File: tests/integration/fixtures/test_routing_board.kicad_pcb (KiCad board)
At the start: 2 copper layers, 3 parts, among them U1 IC1

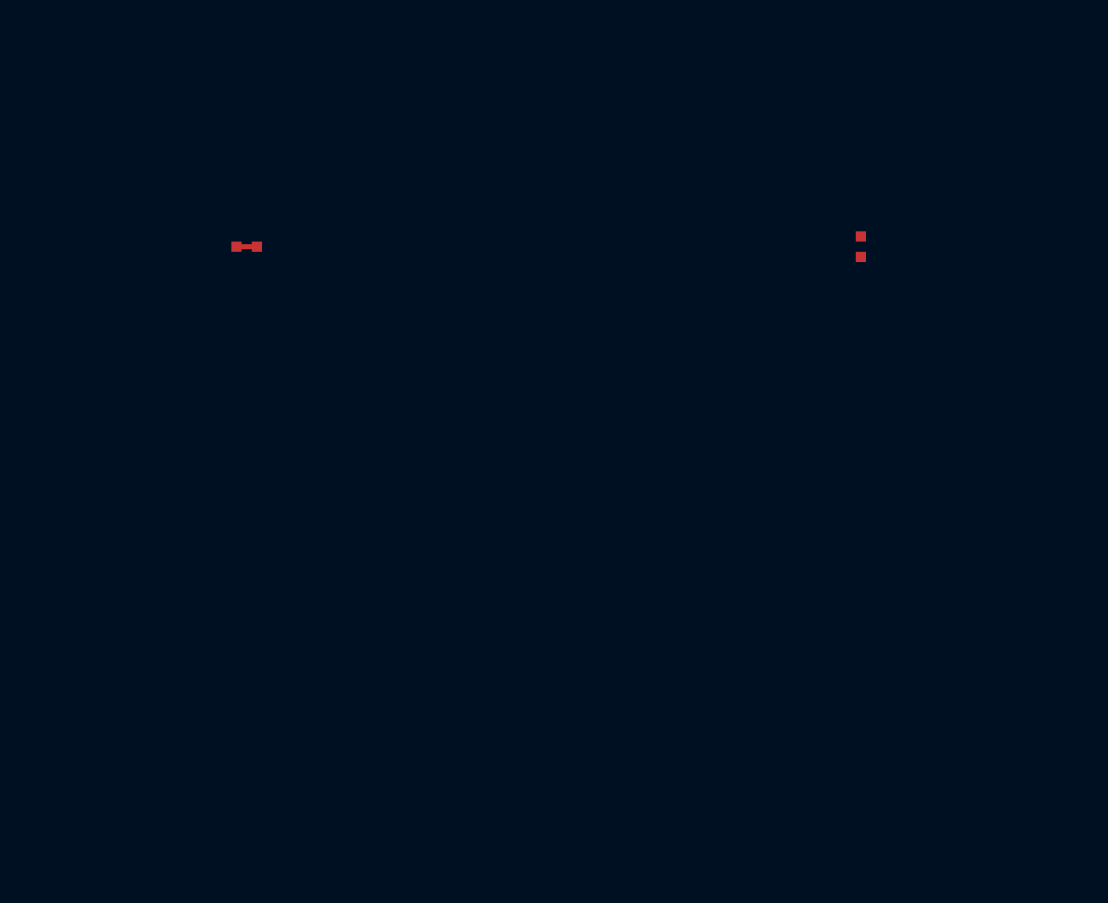
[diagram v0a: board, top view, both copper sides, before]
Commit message: Tighten PNS router error reporting and bounds checking
Replace silent DRC fallbacks with explicit exceptions: the previous
behaviour of _default_track_width and _default_clearance was to swallow
missing or malformed .kicad_pro data and return 0.25 mm / 0.2 mm. That
hides file corruption and makes the AI produce tracks at the wrong
width. Introduce four named exception classes (ProFileMissing,
ProFileMalformed, NetClassUnresolved, DesignRulesUnavailable) and
translate them into RouteFailure with a fix-it hint at the
auto_route_pair boundary. The user can still opt out by passing width=
and clearance= explicitly.

Add _check_segments_in_board and call it after postprocess. When the PCB
has Edge.Cuts, segments whose centerline + width/2 crosses the board
boundary raise RouteFailure (this is a router bug, never papered over).
When Edge.Cuts is absent, log a warning and proceed: the board outline
is a workflow artifact and may legitimately be missing mid-iteration;
KiCad's DRC owns the final validation.

Fixture: add a 50x40 mm gr_rect on Edge.Cuts so the new check is
exercised by the existing integration tests.

Tests: 21 new unit tests in tests/unit/router/test_router.py covering
every DRC exception path, the explicit-override escape hatch, and
boundary / non-boundary / degenerate / too-wide cases for
_check_segments_in_board.

Co-authored-by: Copilot <223556219+Copilot@users.noreply.github.com>

Signed-off-by: paul356 <panhao356@gmail.com>
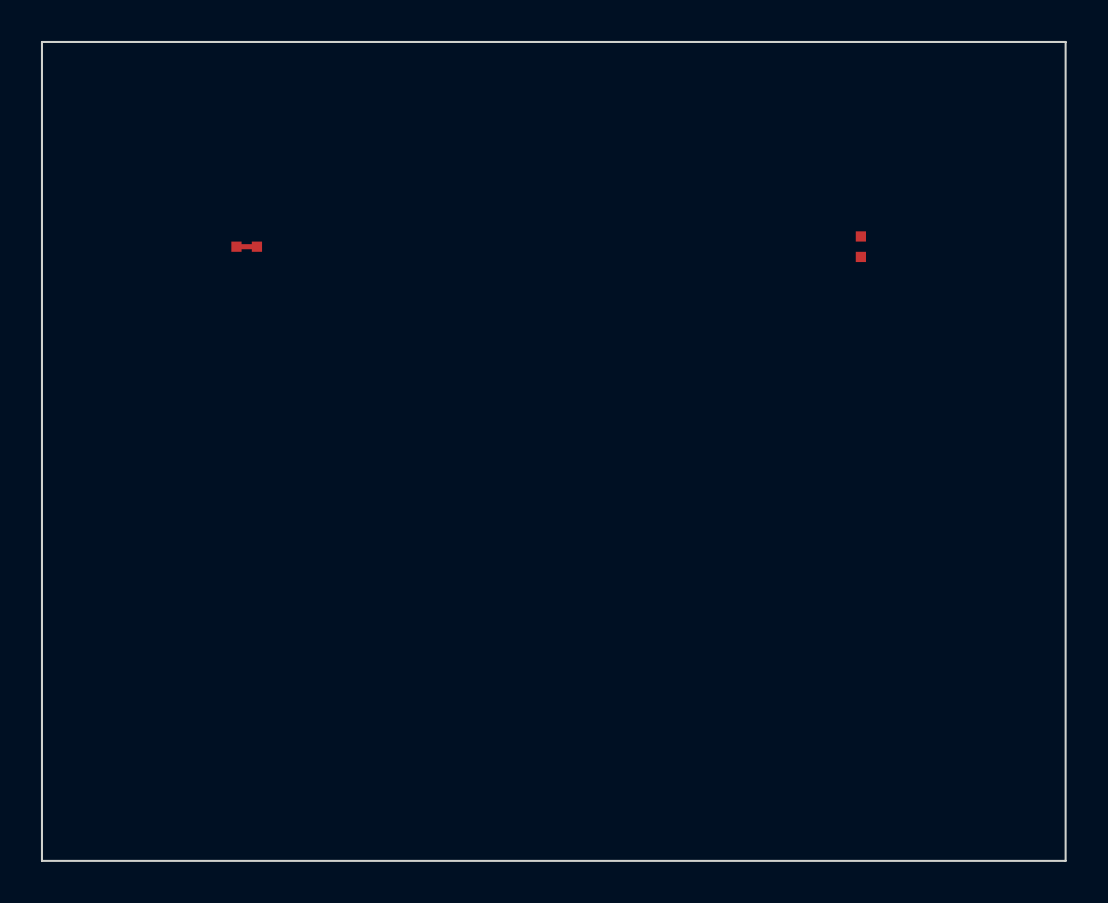
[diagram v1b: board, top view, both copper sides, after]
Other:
- board outline added: 50 x 40 mm
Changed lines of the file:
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@@
 		)
 	)
+	(gr_rect
+		(start 20.0 20.0)
+		(end 70.0 60.0)
+		(stroke
+			(width 0.1)
+			(type solid)
+		)
+		(fill none)
+		(layer "Edge.Cuts")
+		(uuid "edge-cuts-rect-0000")
+	)
 )

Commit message: feat(router): multi-layer MCP tool args + In1.Cu fixture footprint
- pcb_route_pad_to_pad: accept target_layer and via_pairs; emits
  vias in addition to segments; reports layers_used
- fixture: add In1.Cu copper layer and D1 footprint with pad 1 on
  In1.Cu (GND) for cross-layer routing tests

Co-authored-by: Copilot <223556219+Copilot@users.noreply.github.com>

Signed-off-by: paul356 <panhao356@gmail.com>
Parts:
- added D1: D1, Resistor_SMD:R_0402_1005Metric, In1.Cu at (60.0, 50.0)
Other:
- copper layers 2 -> 3
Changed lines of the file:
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@@
 		(0 "F.Cu" signal)
 		(31 "B.Cu" signal)
+		(33 "In1.Cu" signal)
 		(36 "B.Courtyard" user)
 		(37 "F.Courtyard" user)
@@
 		(uuid "edge-cuts-rect-0000")
 	)
+	# ---- D1: SMD pad on In1.Cu (GND) for cross-layer routing tests ----
+	(footprint "Resistor_SMD:R_0402_1005Metric"
+		(layer "In1.Cu")
+		(at 60.0 50.0 0.0)
+		(property "Reference" "D1")
+		(property "Value" "D1")
+		(fp_line
+			(start -1.05 -0.6)
+			(end 1.05 -0.6)
+			(layer "F.CrtYd")
+			(width 0.05)
+		)
+		(fp_line
+			(start 1.05 -0.6)
+			(end 1.05 0.6)
+			(layer "F.CrtYd")
+			(width 0.05)
+		)
+		(fp_line
+			(start 1.05 0.6)
+			(end -1.05 0.6)
+			(layer "F.CrtYd")
+			(width 0.05)
+		)
+		(fp_line
+			(start -1.05 0.6)
+			(end -1.05 -0.6)
+			(layer "F.CrtYd")
+			(width 0.05)
+		)
+		(pad "1" smd rect
+			(at -0.5 0.0)
+			(size 0.5 0.5)
+			(layers "In1.Cu" "B.Paste" "B.Mask")
+			(net 2 "GND")
+		)
+		(pad "2" smd rect
+			(at 0.5 0.0)
+			(size 0.5 0.5)
+			(layers "In1.Cu" "B.Paste" "B.Mask")
+			(net 0 "")
+		)
+	)
 )
